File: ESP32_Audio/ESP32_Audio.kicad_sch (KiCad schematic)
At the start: 23 parts

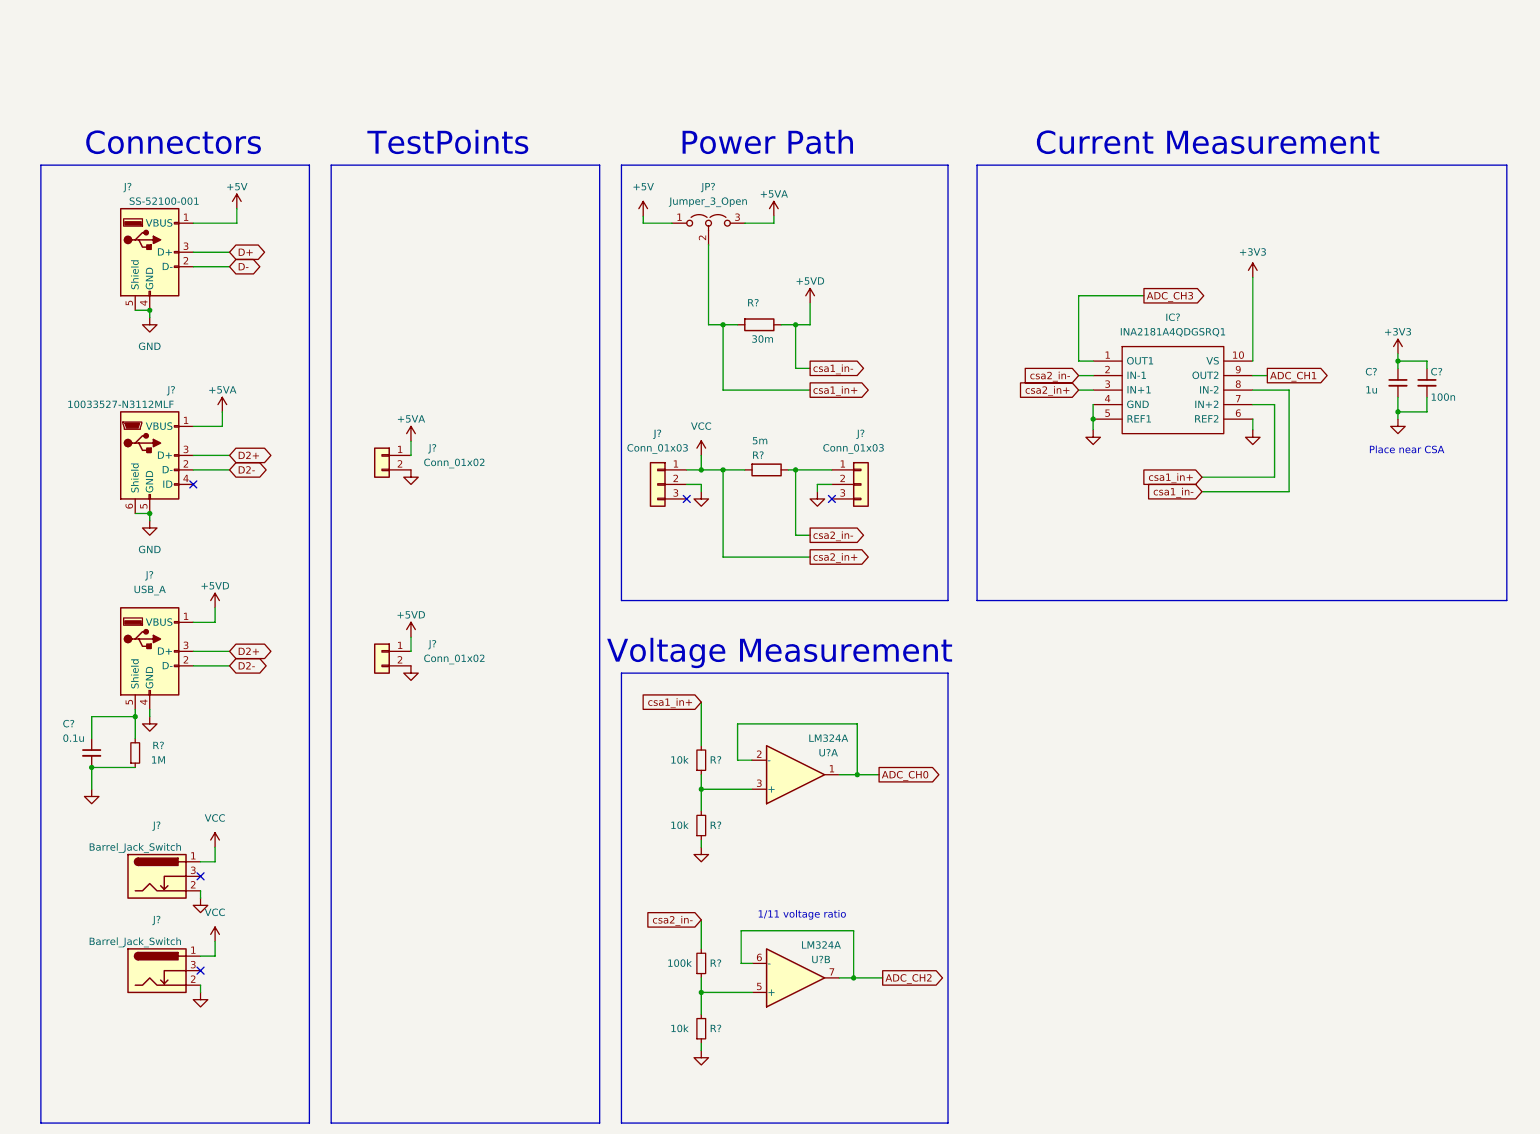
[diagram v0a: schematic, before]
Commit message: Added Li-ion circuit
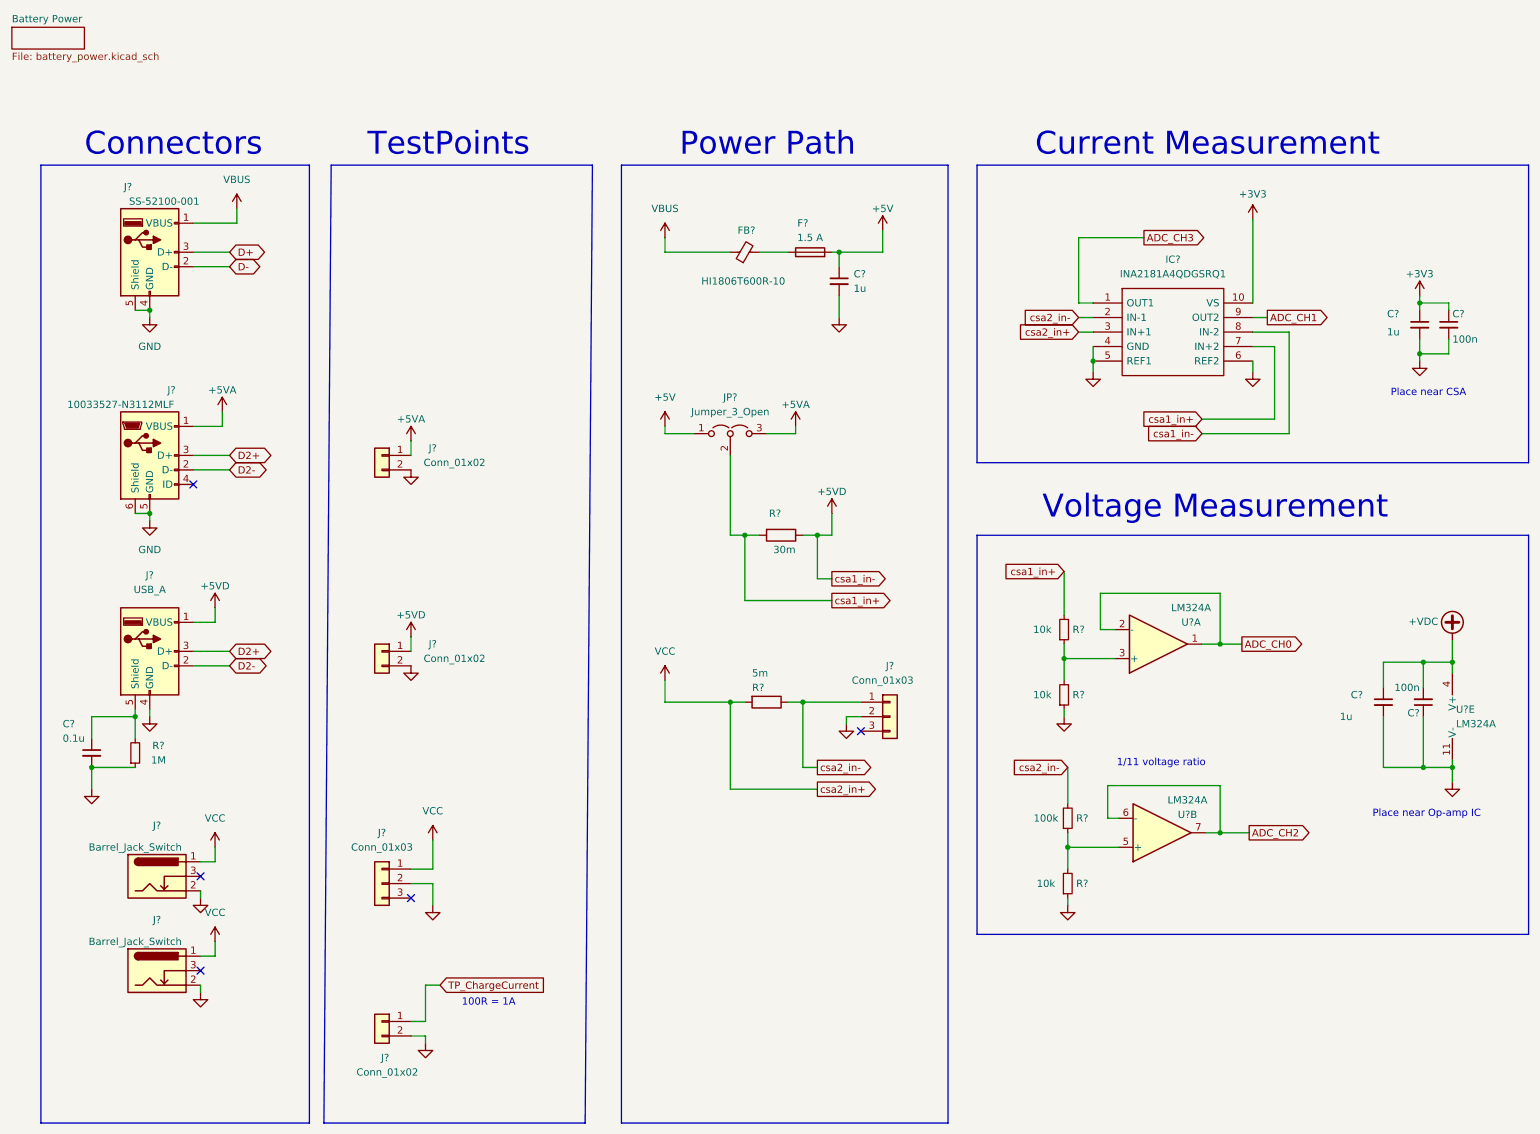
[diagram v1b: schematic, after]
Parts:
- removed J?: Conn_01x03, Connectors:SCREWTERMINAL-5MM-3, symbol Connector_Generic:Conn_01x03
- added C? (x2): 1u, Capacitor_SMD:C_0603_1608Metric_Pad1.08x0.95mm_HandSolder, symbol Device:C_Small
- added C?: 100n, Capacitor_SMD:C_0603_1608Metric_Pad1.08x0.95mm_HandSolder, symbol Device:C_Small
- added F?: 1.5 A, Fuse:Fuse_0603_1608Metric_Pad1.05x0.95mm_HandSolder, symbol Device:Fuse
- added FB?: HI1806T600R-10, SamacSys_Parts:BEADC4516X185N, symbol Device:FerriteBead_Small
- added J?: Conn_01x02, Connector_PinHeader_2.54mm:PinHeader_1x02_P2.54mm_Vertical, symbol Connector_Generic:Conn_01x02
- added J?: Conn_01x03, Connectors:SCREWTERMINAL-5MM-3, symbol Connector_Generic:Conn_01x03
- added U?: LM324A, Package_SO:SOIC-14_3.9x8.7mm_P1.27mm, symbol Amplifier_Operational:LM324A
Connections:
- net +5V: now also C?.1, F?.2; no longer J?.1 (VBUS)
- net GND: now also C?.1, C?.2, C?.2, J?.2 (Pin_2), J?.2 (Pin_2), U?.11 (V-)
- net VCC: now also J?.1 (Pin_1)
- new net: F?.1, FB?.2
- new net +VDC: C?.1, C?.2, U?.4 (V+)
- new net TP_ChargeCurrent: J?.1 (Pin_1)
- new net VBUS: FB?.1, J?.1 (VBUS)
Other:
- added sheet Battery Power (battery_power.kicad_sch)
- note added: "100R = 1A"
- note added: "Place near Op-amp IC"
- moved on the sheet: C?, IC?, J?, JP?, R?, U?A, U?B

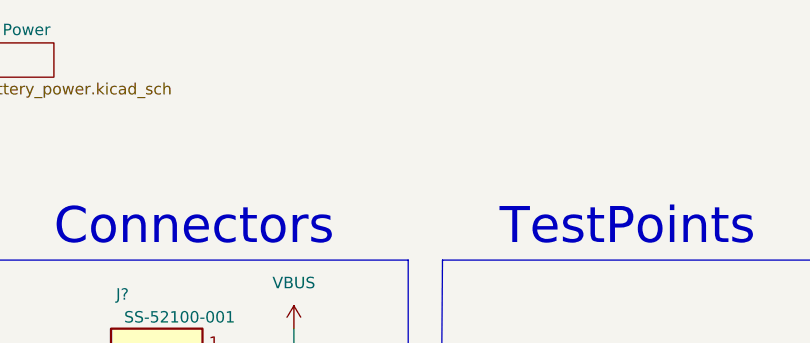
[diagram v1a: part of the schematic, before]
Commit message: Imported LDO library
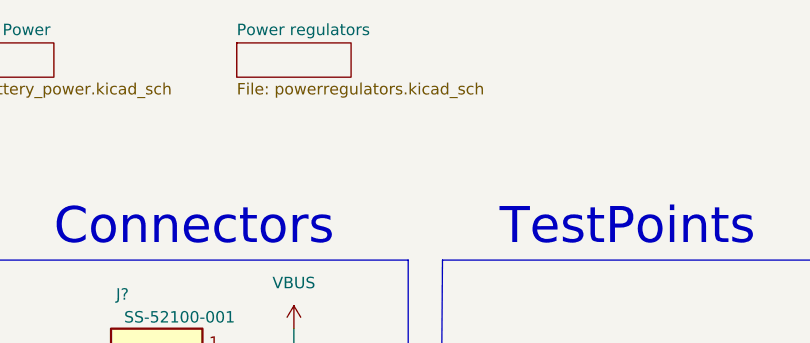
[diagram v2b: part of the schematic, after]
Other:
- added sheet Power regulators (powerregulators.kicad_sch)
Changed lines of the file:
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@@
+    )
+  )
+  (sheet (at 43.18 2.54) (size 12.7 3.81) (fields_autoplaced)
+    (stroke (width 0.1524) (type solid) (color 0 0 0 0))
+    (fill (color 0 0 0 0.0000))
+    (property "Sheet name" "Power regulators" (id 0) (at 43.18 1.8284 0)
+      (effects (font (size 1.27 1.27)) (justify left bottom))
+    )
+    (property "Sheet file" "powerregulators.kicad_sch" (id 1) (at 43.18 6.9346 0)
+      (effects (font (size 1.27 1.27)) (justify left top))
     )
   )
@@
     (path "/" (page "1"))
     (path "/0abae95b-d5a4-4748-82ac-72b4806a03dc" (page "2"))
+    (path "/3841a514-4c7d-4ec2-84d0-06948ce99c88" (page "3"))
   )
   (symbol_instances
@@
       (reference "#PWR?") (unit 1) (value "+5VD") (footprint "")
     )
+    (path "/3841a514-4c7d-4ec2-84d0-06948ce99c88/35d426ba-7bfb-42fd-b324-993fcbe58b20"
+      (reference "#PWR?") (unit 1) (value "GND") (footprint "")
+    )
     (path "/0abae95b-d5a4-4748-82ac-72b4806a03dc/3647b579-9f04-4867-ad80-87ffc46424d4"
       (reference "#PWR?") (unit 1) (value "GND") (footprint "")
@@
       (reference "#PWR?") (unit 1) (value "+5VA") (footprint "")
     )
-    (path "/0abae95b-d5a4-4748-82ac-72b4806a03dc/80be51b0-d28a-42ba-94ba-5266eb731e91"
-      (reference "#PWR?") (unit 1) (value "GND") (footprint "")
-    )
     (path "/80fce06e-7e63-4980-af2b-58dc44402d67"
       (reference "#PWR?") (unit 1) (value "+3V3") (footprint "")
@@
       (reference "#PWR?") (unit 1) (value "GND") (footprint "")
     )
+    (path "/3841a514-4c7d-4ec2-84d0-06948ce99c88/c9517de9-e596-4a78-8ef5-71f63dba7571"
+      (reference "#PWR?") (unit 1) (value "GND") (footprint "")
+    )
+    (path "/3841a514-4c7d-4ec2-84d0-06948ce99c88/ca3e7f10-e5c3-4276-a2ce-21d7ec249758"
+      (reference "#PWR?") (unit 1) (value "GND") (footprint "")
+    )
     (path "/0abae95b-d5a4-4748-82ac-72b4806a03dc/cb0c6afa-66d7-4c36-985e-6a58a9e15f2c"
+      (reference "#PWR?") (unit 1) (value "GND") (footprint "")
+    )
+    (path "/3841a514-4c7d-4ec2-84d0-06948ce99c88/ce6ad3bc-e0b4-4e89-b898-344d0f76d5aa"
       (reference "#PWR?") (unit 1) (value "GND") (footprint "")
     )
@@
       (reference "#PWR?") (unit 1) (value "+5VA") (footprint "")
     )
+    (path "/3841a514-4c7d-4ec2-84d0-06948ce99c88/fe1ef6b4-74d3-43c6-9304-4a8e6e477d2c"
+      (reference "#PWR?") (unit 1) (value "+VDC") (footprint "")
+    )
     (path "/fe6a3f98-3826-4734-8e13-6f07b97ef0a6"
       (reference "#PWR?") (unit 1) (value "GND") (footprint "")
@@
       (reference "#PWR?") (unit 1) (value "VCC") (footprint "")
     )
+    (path "/3841a514-4c7d-4ec2-84d0-06948ce99c88/082f9ef8-e3a1-4eb3-9bf6-3517f915e0c7"
+      (reference "C?") (unit 1) (value "1u") (footprint "Capacitor_SMD:C_0805_2012Metric_Pad1.18x1.45mm_HandSolder")
+    )
+    (path "/3841a514-4c7d-4ec2-84d0-06948ce99c88/11147381-71ed-4c20-a6fa-a9ed6d0e71c8"
+      (reference "C?") (unit 1) (value "1u") (footprint "Capacitor_SMD:C_0805_2012Metric_Pad1.18x1.45mm_HandSolder")
+    )
     (path "/0abae95b-d5a4-4748-82ac-72b4806a03dc/2e358f81-0ec0-4327-85ce-b1f039f408a8"
       (reference "C?") (unit 1) (value "1u") (footprint "Capacitor_SMD:C_0603_1608Metric_Pad1.08x0.95mm_HandSolder")
@@
       (reference "R?") (unit 1) (value "470") (footprint "Resistor_SMD:R_0603_1608Metric_Pad0.98x0.95mm_HandSolder")
     )
-    (path "/0abae95b-d5a4-4748-82ac-72b4806a03dc/0cd50f23-d3cf-4e54-a487-9dcc58791ed0"
-      (reference "R?") (unit 1) (value "10k") (footprint "Resistor_SMD:R_0603_1608Metric_Pad0.98x0.95mm_HandSolder")
-    )
     (path "/109a32ec-3752-47da-87ed-db30f98606df"
       (reference "R?") (unit 1) (value "100k") (footprint "Resistor_SMD:R_0603_1608Metric_Pad0.98x0.95mm_HandSolder")
@@
       (reference "R?") (unit 1) (value "10k") (footprint "Resistor_SMD:R_0603_1608Metric_Pad0.98x0.95mm_HandSolder")
     )
-    (path "/0abae95b-d5a4-4748-82ac-72b4806a03dc/7a332880-b6be-4e69-ba8a-52c3f7735500"
-      (reference "R?") (unit 1) (value "10k") (footprint "Resistor_SMD:R_0603_1608Metric_Pad0.98x0.95mm_HandSolder")
-    )
     (path "/0abae95b-d5a4-4748-82ac-72b4806a03dc/87f7e3cb-84c3-4770-a11c-d49589877ddd"
       (reference "R?") (unit 1) (value "100k") (footprint "Resistor_SMD:R_0603_1608Metric_Pad0.98x0.95mm_HandSolder")
@@
       (reference "RV?") (unit 1) (value "10k") (footprint "Potentiometer_THT:Potentiometer_Bourns_3386F_Vertical")
     )
+    (path "/3841a514-4c7d-4ec2-84d0-06948ce99c88/0fad01c3-c621-4b29-b9c8-abc38a977e63"
+      (reference "U?") (unit 1) (value "AP2112M-3.3TRG1") (footprint "AP2112M-3.3TRG1:SOIC127P600X175-8N")
+    )
     (path "/15f560b6-5f77-4d15-b789-d3c7a6b8170c"
